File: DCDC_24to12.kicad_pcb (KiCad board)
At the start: 2 copper layers, 28 parts, among them J1 Power_IN, J2 Power_OUT, U1 BD9F800MUX-ZE2

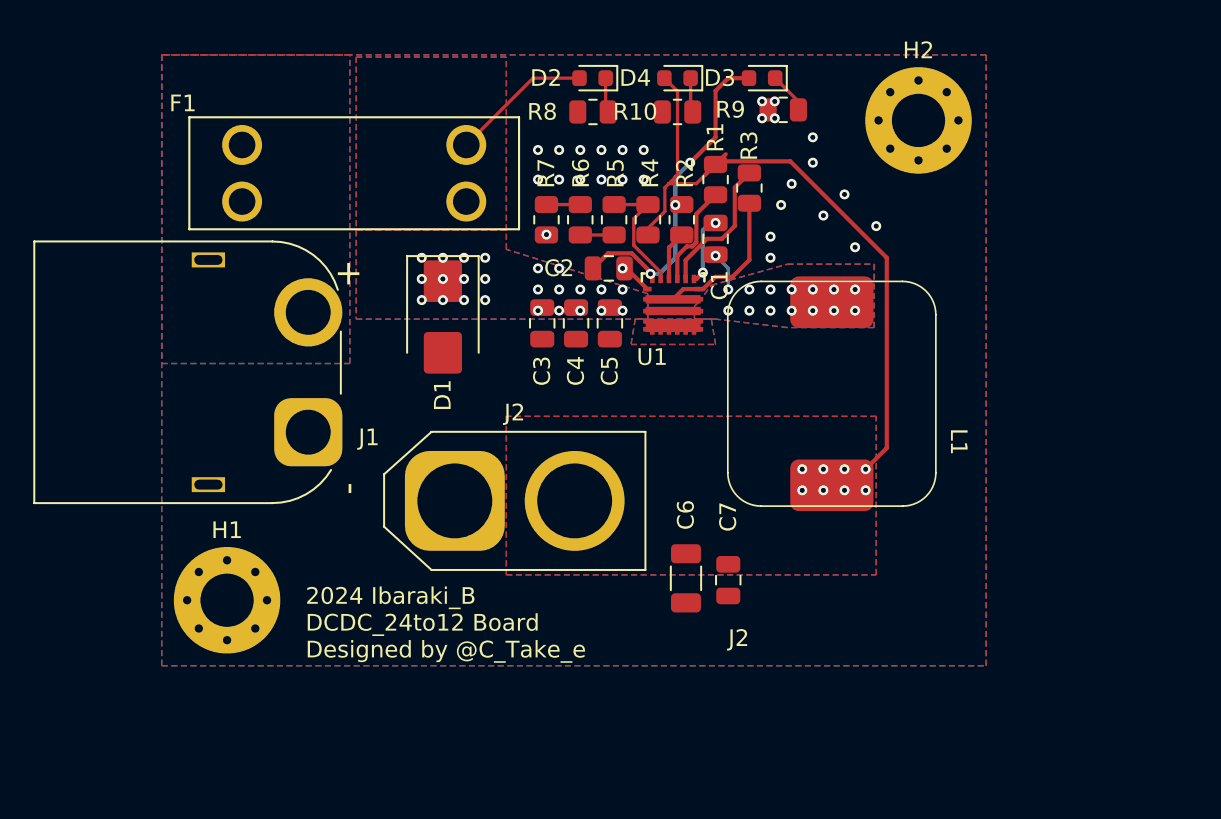
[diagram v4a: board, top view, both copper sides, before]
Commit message: 外形とか配線とかビアとか整頓
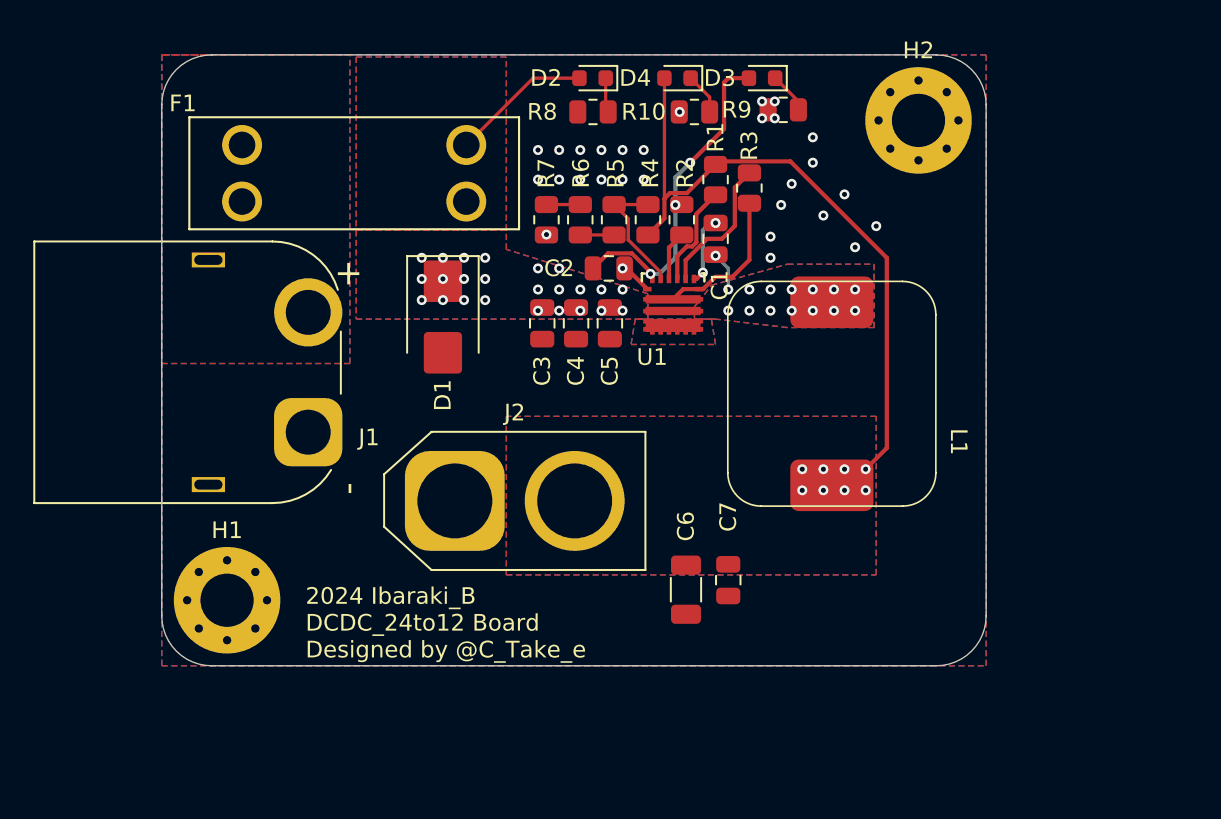
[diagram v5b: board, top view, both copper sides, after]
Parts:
- moved R10 1.02 mm to (103.4, 42.7)
- moved C6 0.68 mm to (102.9, 71.4)
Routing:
- net +12V: track 40.5 -> 39.8 mm
- net GND: vias 28 -> 29
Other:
- board outline added: 49.5 x 36.7 mm
- board text removed: "J2"
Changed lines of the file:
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@@
 	(footprint "Capacitor_SMD:C_1206_3216Metric"
 		(layer "F.Cu")
-		(at 102.87 70.69 -90)
+		(at 102.87 71.374 -90)
 		(descr "Capacitor SMD 1206 (3216 Metric), square (rectangular) end terminal, IPC_7351 nominal, (Body size source: IPC-SM-782 page 76, https://www.pcb-3d.com/wordpress/wp-content/uploads/ipc-sm-782a_amendment_1_and_2.pdf), generated with kicad-footprint-generator")
 		(tags "capacitor")
@@
 		(tags "resistor")
 		(property "Reference" "R9"
-			(at 3.175 0 0)
+			(at 2.794 0 0)
 			(layer "F.SilkS")
 			(effects
@@
 	(footprint "Resistor_SMD:R_0805_2012Metric"
 		(layer "F.Cu")
-		(at 102.362 42.672 180)
+		(at 103.378 42.672 180)
 		(descr "Resistor SMD 0805 (2012 Metric), square (rectangular) end terminal, IPC_7351 nominal, (Body size source: IPC-SM-782 page 72, https://www.pcb-3d.com/wordpress/wp-content/uploads/ipc-sm-782a_amendment_1_and_2.pdf), generated with kicad-footprint-generator")
 		(tags "resistor")
 		(property "Reference" "R10"
-			(at 2.54 0 0)
+			(at 3.048 0 0)
 			(layer "F.SilkS")
 			(effects
@@
 		(layer "F.Mask")
 	)
+	(gr_arc
+		(start 120.904 72.946)
+		(mid 120.02532 75.06732)
+		(end 117.904 75.946)
+		(stroke
+			(width 0.05)
+			(type default)
+		)
+		(layer "Edge.Cuts")
+	)
+	(gr_arc
+		(start 71.374 42.243)
+		(mid 72.25268 40.12168)
+		(end 74.374 39.243)
+		(stroke
+			(width 0.05)
+			(type default)
+		)
+		(layer "Edge.Cuts")
+	)
+	(gr_line
+		(start 71.374 72.946)
+		(end 71.374 42.243)
+		(stroke
+			(width 0.05)
+			(type default)
+		)
+		(layer "Edge.Cuts")
+	)
+	(gr_arc
+		(start 74.374 75.946)
+		(mid 72.25268 75.06732)
+		(end 71.374 72.946)
+		(stroke
+			(width 0.05)
+			(type default)
+		)
+		(layer "Edge.Cuts")
+	)
+	(gr_line
+		(start 74.374 39.243)
+		(end 117.904 39.243)
+		(stroke
+			(width 0.05)
+			(type default)
+		)
+		(layer "Edge.Cuts")
+	)
+	(gr_line
+		(start 117.904 75.946)
+		(end 74.374 75.946)
+		(stroke
+			(width 0.05)
+			(type default)
+		)
+		(layer "Edge.Cuts")
+	)
+	(gr_line
+		(start 120.904 42.243)
+		(end 120.904 72.946)
+		(stroke
+			(width 0.05)
+			(type default)
+		)
+		(layer "Edge.Cuts")
+	)
+	(gr_arc
+		(start 117.904 39.243)
+		(mid 120.02532 40.12168)
+		(end 120.904 42.243)
+		(stroke
+			(width 0.05)
+			(type default)
+		)
+		(layer "Edge.Cuts")
+	)
 	(gr_text "2024 Ibaraki_B\nDCDC_24to12 Board\nDesigned by @C_Take_e"
 		(at 80.01 75.565 0)
@@
 		)
 	)
-	(gr_text "J2"
-		(at 106.045 74.295 0)
-		(layer "F.SilkS")
-		(effects
-			(font
-				(size 1 1)
-				(thickness 0.15)
+	(dimension
+		(type aligned)
+		(layer "Cmts.User")
+		(pts
+			(xy 120.904 75.946) (xy 71.374 75.946)
+		)
+		(height -6.858)
+		(gr_text "49.5300 mm"
+			(at 96.139 81.654 0)
+			(layer "Cmts.User")
+			(effects
+				(font
+					(size 1 1)
+					(thickness 0.15)
+				)
+			)
+		)
+		(format
+			(prefix "")
+			(suffix "")
+			(units 3)
+			(units_format 1)
+			(precision 4)
+		)
+		(style
+			(thickness 0.1)
+			(arrow_length 1.27)
+			(text_position_mode 0)
+			(extension_height 0.58642)
+			(extension_offset 0.5) keep_text_aligned)
+	)
+	(dimension
+		(type aligned)
+		(layer "Cmts.User")
+		(pts
+			(xy 120.904 75.946) (xy 120.904 39.243)
+		)
+		(height 7.493)
+		(gr_text "36.7030 mm"
+			(at 127.247 57.5945 90)
+			(layer "Cmts.User")
+			(effects
+				(font
+					(size 1 1)
+					(thickness 0.15)
+				)
 			)
 		)
+		(format
+			(prefix "")
+			(suffix "")
+			(units 3)
+			(units_format 1)
+			(precision 4)
+		)
+		(style
+			(thickness 0.1)
+			(arrow_length 1.27)
+			(text_position_mode 0)
+			(extension_height 0.58642)
+			(extension_offset 0.5) keep_text_aligned)
 	)
 	(segment
@@
 	)
 	(via
+		(at 102.489 42.672)
+		(size 0.6)
+		(drill 0.3)
+		(layers "F.Cu" "B.Cu")
+		(net 1)
+	)
+	(via
 		(at 96.52 46.736)
 		(size 0.6)
@@
 	)
 	(segment
-		(start 101.6 48.653763)
-		(end 100.388131 49.865632)
-		(width 0.2)
-		(layer "F.Cu")
-		(net 2)
-	)
-	(segment
-		(start 104.648 45.8235)
-		(end 105.2595 45.212)
-		(width 0.254)
-		(layer "F.Cu")
-		(net 2)
-	)
-	(segment
-		(start 104.648 45.8235)
-		(end 104.013 46.4585)
-		(width 0.254)
-		(layer "F.Cu")
-		(net 2)
-	)
-	(segment
 		(start 104.8295 45.642)
 		(end 109.142 45.642)
@@
 	)
 	(segment
-		(start 101.84225 46.97825)
-		(end 101.6 47.2205)
-		(width 0.2)
+		(start 101.5745 49.071)
+		(end 100.584 50.0615)
+		(width 0.254)
 		(layer "F.Cu")
 		(net 2)
@@
 	)
 	(segment
-		(start 102.362 46.4585)
-		(end 101.84225 46.97825)
-		(width 0.2)
-		(layer "F.Cu")
-		(net 2)
-	)
-	(segment
 		(start 109.142 45.642)
 		(end 114.935 51.435)
@@
 	)
 	(segment
-		(start 114.935 62.865)
-		(end 113.665 64.135)
-		(width 0.254)
+		(start 101.5745 40.64)
+		(end 101.5745 47.879)
+		(width 0.2)
 		(layer "F.Cu")
 		(net 2)
 	)
 	(segment
-		(start 101.6 47.2205)
-		(end 101.6 48.653763)
-		(width 0.2)
+		(start 101.9065 47.547)
+		(end 101.5745 47.879)
+		(width 0.254)
 		(layer "F.Cu")
 		(net 2)
 	)
 	(segment
-		(start 102.362 41.4275)
-		(end 102.362 46.4585)
-		(width 0.2)
+		(start 114.935 62.865)
+		(end 113.665 64.135)
+		(width 0.254)
 		(layer "F.Cu")
 		(net 2)
 	)
 	(segment
-		(start 101.5745 40.64)
-		(end 102.362 41.4275)
-		(width 0.2)
+		(start 102.9245 47.547)
+		(end 101.9065 47.547)
+		(width 0.254)
 		(layer "F.Cu")
 		(net 2)
 	)
 	(segment
-		(start 101.84225 46.97825)
-		(end 103.49325 46.97825)
-		(width 0.2)
+		(start 104.648 45.8235)
+		(end 102.9245 47.547)
+		(width 0.254)
 		(layer "F.Cu")
 		(net 2)
 	)
 	(segment
-		(start 103.49325 46.97825)
-		(end 104.013 46.4585)
-		(width 0.2)
+		(start 101.5745 47.879)
+		(end 101.5745 49.071)
+		(width 0.254)
 		(layer "F.Cu")
 		(net 2)
@@
 	)
 	(segment
-		(start 103.1495 42.547)
-		(end 103.1495 40.64)
+		(start 104.2905 42.672)
+		(end 104.2905 41.781)
 		(width 0.2)
 		(layer "F.Cu")
@@
 	)
 	(segment
-		(start 103.2745 42.672)
-		(end 103.1495 42.547)
+		(start 104.2905 41.781)
+		(end 103.1495 40.64)
 		(width 0.2)
 		(layer "F.Cu")
@@
 	)
 	(segment
-		(start 99.734 50.690693)
-		(end 101.347811 52.304504)
+		(start 101.347811 52.304504)
+		(end 101.347811 52.705)
 		(width 0.2)
 		(layer "F.Cu")
@@
 	)
 	(segment
-		(start 99.734 49.0865)
-		(end 99.734 50.690693)
+		(start 98.552 48.2365)
+		(end 99.402 49.0865)
 		(width 0.2)
 		(layer "F.Cu")
@@
 	)
 	(segment
-		(start 100.584 48.2365)
-		(end 98.552 48.2365)
+		(start 99.402 49.0865)
+		(end 99.402 50.358693)
 		(width 0.2)
 		(layer "F.Cu")
@@
 	(segment
 		(start 100.584 48.2365)
-		(end 99.734 49.0865)
+		(end 98.552 48.2365)
 		(width 0.2)
 		(layer "F.Cu")
@@
 	)
 	(segment
-		(start 101.347811 52.304504)
-		(end 101.347811 52.705)
+		(start 99.402 50.358693)
+		(end 101.347811 52.304504)
 		(width 0.2)
 		(layer "F.Cu")
@@
 	)
 	(segment
-		(start 100.847685 52.511485)
-		(end 100.847685 52.705)
+		(start 105.41 40.64)
+		(end 106.6545 40.64)
 		(width 0.254)
 		(layer "F.Cu")
@@
 	)
 	(segment
-		(start 104.648 44.196)
-		(end 104.648 41.402)
+		(start 100.847685 52.511485)
+		(end 100.847685 52.705)
 		(width 0.254)
 		(layer "F.Cu")
@@
 	)
 	(segment
-		(start 100.7364 52.288606)
-		(end 99.615794 51.168)
+		(start 103.124 45.72)
+		(end 105.156 43.688)
 		(width 0.254)
 		(layer "F.Cu")
@@
 	)
 	(segment
-		(start 98.184 51.168)
-		(end 97.282 52.07)
+		(start 105.156 43.688)
+		(end 105.156 40.894)
 		(width 0.254)
 		(layer "F.Cu")
@@
 	)
 	(segment
-		(start 104.648 41.402)
-		(end 105.41 40.64)
+		(start 100.7364 52.288606)
+		(end 99.615794 51.168)
 		(width 0.254)
 		(layer "F.Cu")
@@
 	)
 	(segment
-		(start 99.615794 51.168)
-		(end 98.184 51.168)
+		(start 98.184 51.168)
+		(end 97.282 52.07)
 		(width 0.254)
 		(layer "F.Cu")
@@
 	)
 	(segment
-		(start 105.41 40.64)
-		(end 106.6545 40.64)
+		(start 99.615794 51.168)
+		(end 98.184 51.168)
 		(width 0.254)
 		(layer "F.Cu")
@@
 	)
 	(segment
-		(start 103.124 45.72)
-		(end 104.648 44.196)
+		(start 105.156 40.894)
+		(end 105.41 40.64)
 		(width 0.254)
 		(layer "F.Cu")

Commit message: 出力コンデンサ位置修正
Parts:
- moved C6 8.52 mm to (101.0, 63.1), turned to 90 degrees
- moved C7 7.54 mm to (103.5, 63.5), turned to 90 degrees
- moved J2 2.34 mm to (87.6, 67.9)
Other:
- board text added: "363mm^2"
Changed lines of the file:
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@@
 	(footprint "Capacitor_SMD:C_0805_2012Metric"
 		(layer "F.Cu")
-		(at 105.41 70.8 -90)
+		(at 103.505 63.5 90)
 		(descr "Capacitor SMD 0805 (2012 Metric), square (rectangular) end terminal, IPC_7351 nominal, (Body size source: IPC-SM-782 page 76, https://www.pcb-3d.com/wordpress/wp-content/uploads/ipc-sm-782a_amendment_1_and_2.pdf, https://docs.google.com/spreadsheets/d/1BsfQQcO9C6DZCsRaXUlFlo91Tg2WpOkGARC1WS5S8t0/edit?usp=sharing), generated with kicad-footprint-generator")
 		(tags "capacitor")
 		(property "Reference" "C7"
-			(at -3.81 0 90)
+			(at -3.175 0 90)
 			(layer "F.SilkS")
 			(effects
@@
 		)
 		(property "Footprint" "Capacitor_SMD:C_0805_2012Metric"
-			(at 0 0 -90)
+			(at 0 0 90)
 			(unlocked yes)
 			(layer "F.Fab")
@@
 		)
 		(property "Datasheet" ""
-			(at 0 0 -90)
+			(at 0 0 90)
 			(unlocked yes)
 			(layer "F.Fab")
@@
 		)
 		(property "Description" "Unpolarized capacitor, small symbol"
-			(at 0 0 -90)
+			(at 0 0 90)
 			(unlocked yes)
 			(layer "F.Fab")
@@
 		(attr smd)
 		(fp_line
-			(start -0.261252 0.735)
-			(end 0.261252 0.735)
+			(start -0.261252 -0.735)
+			(end 0.261252 -0.735)
 			(stroke
 				(width 0.12)
@@
 		)
 		(fp_line
-			(start -0.261252 -0.735)
-			(end 0.261252 -0.735)
+			(start -0.261252 0.735)
+			(end 0.261252 0.735)
 			(stroke
 				(width 0.12)
@@
 		)
 		(fp_line
-			(start -1.7 0.98)
-			(end -1.7 -0.98)
+			(start 1.7 -0.98)
+			(end 1.7 0.98)
 			(stroke
 				(width 0.05)
@@
 		)
 		(fp_line
-			(start 1.7 0.98)
-			(end -1.7 0.98)
+			(start -1.7 -0.98)
+			(end 1.7 -0.98)
 			(stroke
 				(width 0.05)
@@
 		)
 		(fp_line
-			(start -1.7 -0.98)
-			(end 1.7 -0.98)
+			(start 1.7 0.98)
+			(end -1.7 0.98)
 			(stroke
 				(width 0.05)
@@
 		)
 		(fp_line
-			(start 1.7 -0.98)
-			(end 1.7 0.98)
+			(start -1.7 0.98)
+			(end -1.7 -0.98)
 			(stroke
 				(width 0.05)
@@
 		)
 		(fp_line
-			(start -1 0.625)
-			(end -1 -0.625)
+			(start 1 -0.625)
+			(end 1 0.625)
 			(stroke
 				(width 0.1)
@@
 		)
 		(fp_line
-			(start 1 0.625)
-			(end -1 0.625)
+			(start -1 -0.625)
+			(end 1 -0.625)
 			(stroke
 				(width 0.1)
@@
 		)
 		(fp_line
-			(start -1 -0.625)
-			(end 1 -0.625)
+			(start 1 0.625)
+			(end -1 0.625)
 			(stroke
 				(width 0.1)
@@
 		)
 		(fp_line
-			(start 1 -0.625)
-			(end 1 0.625)
+			(start -1 0.625)
+			(end -1 -0.625)
 			(stroke
 				(width 0.1)
@@
 		)
 		(pad "1" smd roundrect
-			(at -0.95 0 270)
+			(at -0.95 0 90)
 			(size 1 1.45)
 			(layers "F.Cu" "F.Paste" "F.Mask")
@@
 		)
 		(pad "2" smd roundrect
-			(at 0.95 0 270)
+			(at 0.95 0 90)
 			(size 1 1.45)
 			(layers "F.Cu" "F.Paste" "F.Mask")
@@
 		(tags "mounting hole 3.2mm m3")
 		(property "Reference" "H2"
-			(at 0 -4.2 0)
+			(at -5.08 -1.905 0)
 			(layer "F.SilkS")
 			(effects
@@
 	(footprint "Capacitor_SMD:C_1206_3216Metric"
 		(layer "F.Cu")
-		(at 102.87 71.374 -90)
+		(at 100.965 63.07 90)
 		(descr "Capacitor SMD 1206 (3216 Metric), square (rectangular) end terminal, IPC_7351 nominal, (Body size source: IPC-SM-782 page 76, https://www.pcb-3d.com/wordpress/wp-content/uploads/ipc-sm-782a_amendment_1_and_2.pdf), generated with kicad-footprint-generator")
 		(tags "capacitor")
 		(property "Reference" "C6"
-			(at -3.81 0 90)
+			(at -3.605 0 90)
 			(layer "F.SilkS")
 			(effects
@@
 		)
 		(property "Footprint" "Capacitor_SMD:C_1206_3216Metric"
-			(at 0 0 -90)
+			(at 0 0 90)
 			(unlocked yes)
 			(layer "F.Fab")
@@
 		)
 		(property "Datasheet" ""
-			(at 0 0 -90)
+			(at 0 0 90)
 			(unlocked yes)
 			(layer "F.Fab")
@@
 		)
 		(property "Description" "Unpolarized capacitor, small symbol"
-			(at 0 0 -90)
+			(at 0 0 90)
 			(unlocked yes)
 			(layer "F.Fab")
@@
 		(attr smd)
 		(fp_line
-			(start -0.711252 0.91)
-			(end 0.711252 0.91)
+			(start -0.711252 -0.91)
+			(end 0.711252 -0.91)
 			(stroke
 				(width 0.12)
@@
 		)
 		(fp_line
-			(start -0.711252 -0.91)
-			(end 0.711252 -0.91)
+			(start -0.711252 0.91)
+			(end 0.711252 0.91)
 			(stroke
 				(width 0.12)
@@
 		)
 		(fp_line
-			(start -2.3 1.15)
-			(end -2.3 -1.15)
+			(start 2.3 -1.15)
+			(end 2.3 1.15)
 			(stroke
 				(width 0.05)
@@
 		)
 		(fp_line
-			(start 2.3 1.15)
-			(end -2.3 1.15)
+			(start -2.3 -1.15)
+			(end 2.3 -1.15)
 			(stroke
 				(width 0.05)
@@
 		)
 		(fp_line
-			(start -2.3 -1.15)
-			(end 2.3 -1.15)
+			(start 2.3 1.15)
+			(end -2.3 1.15)
 			(stroke
 				(width 0.05)
@@
 		)
 		(fp_line
-			(start 2.3 -1.15)
-			(end 2.3 1.15)
+			(start -2.3 1.15)
+			(end -2.3 -1.15)
 			(stroke
 				(width 0.05)
@@
 		)
 		(fp_line
-			(start -1.6 0.8)
-			(end -1.6 -0.8)
+			(start 1.6 -0.8)
+			(end 1.6 0.8)
 			(stroke
 				(width 0.1)
@@
 		)
 		(fp_line
-			(start 1.6 0.8)
-			(end -1.6 0.8)
+			(start -1.6 -0.8)
+			(end 1.6 -0.8)
 			(stroke
 				(width 0.1)
@@
 		)
 		(fp_line
-			(start -1.6 -0.8)
-			(end 1.6 -0.8)
+			(start 1.6 0.8)
+			(end -1.6 0.8)
 			(stroke
 				(width 0.1)
@@
 		)
 		(fp_line
-			(start 1.6 -0.8)
-			(end 1.6 0.8)
+			(start -1.6 0.8)
+			(end -1.6 -0.8)
 			(stroke
 				(width 0.1)
@@
 		)
 		(pad "1" smd roundrect
-			(at -1.475 0 270)
+			(at -1.475 0 90)
 			(size 1.15 1.8)
 			(layers "F.Cu" "F.Paste" "F.Mask")
@@
 		)
 		(pad "2" smd roundrect
-			(at 1.475 0 270)
+			(at 1.475 0 90)
 			(size 1.15 1.8)
 			(layers "F.Cu" "F.Paste" "F.Mask")
@@
 	(footprint "Connector_AMASS:AMASS_XT60-F_1x02_P7.20mm_Vertical"
 		(layer "F.Cu")
-		(at 88.983 66.04)
+		(at 87.63 67.945)
 		(descr "AMASS female XT60, through hole, vertical, https://www.tme.eu/Document/2d152ced3b7a446066e6c419d84bb460/XT60%20SPEC.pdf")
 		(tags "XT60 female vertical")
@@
 	)
 	(gr_text "2024 Ibaraki_B\nDCDC_24to12 Board\nDesigned by @C_Take_e"
-		(at 80.01 75.565 0)
+		(at 100.965 74.295 0)
 		(layer "F.SilkS")
 		(effects
@@
 		)
 	)
+	(gr_text "363mm^2"
+		(at 90.805 60.96 0)
+		(layer "Cmts.User")
+		(effects
+			(font
+				(size 1 1)
+				(thickness 0.1)
+			)
+			(justify left bottom)
+		)
+	)
 	(dimension
 		(type aligned)
@@
 		(polygon
 			(pts
-				(xy 92.075 60.96) (xy 92.075 70.485) (xy 114.3 70.485) (xy 114.3 60.96)
+				(xy 90.805 63.5) (xy 90.805 71.755) (xy 114.3 71.755) (xy 114.3 63.5)
 			)
 		)
